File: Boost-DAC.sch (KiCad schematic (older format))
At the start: 26 parts, among them Q17 BSZ100N06NSATMA1, U6 LTC3873, U7 MAX5215

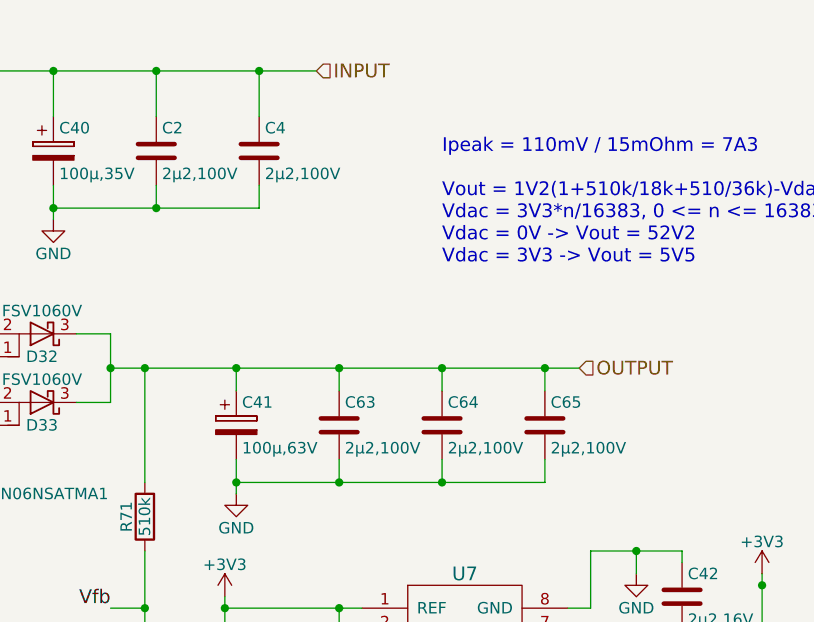
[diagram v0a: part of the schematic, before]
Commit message: 0.2 HW files finalized and repo cleaned up.
-BOM is now up-to-date and available in .csv and .pdf formats
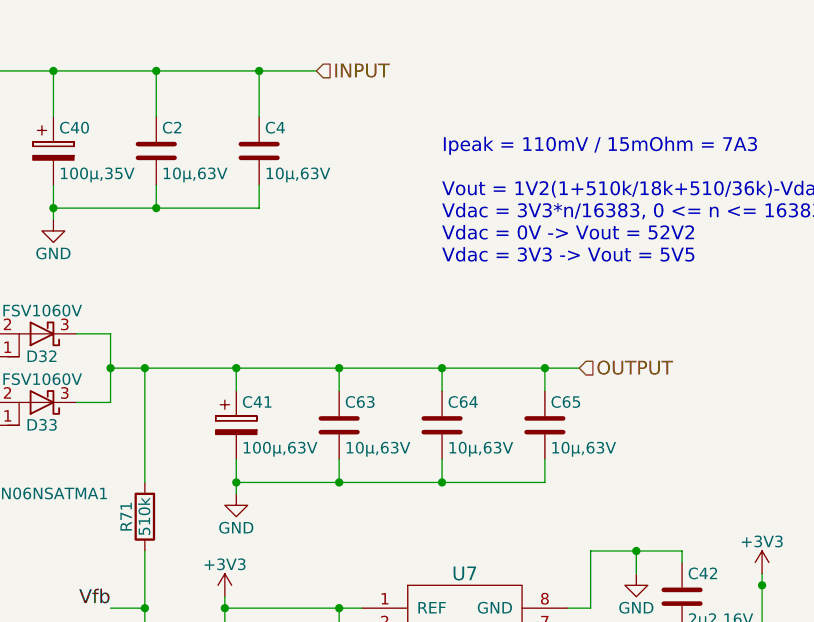
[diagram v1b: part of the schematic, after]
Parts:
- C2, C4, C63, C64, C65: value 2µ2,100V -> 10µ,63V; MFG HMK325B7225MM-P -> ANY
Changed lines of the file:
@@
 P 6450 3550
 F 0 "C63" H 6475 3650 50  0000 L CNN
-F 1 "2µ2,100V" H 6475 3450 50  0000 L CNN
+F 1 "10µ,63V" H 6475 3450 50  0000 L CNN
 F 2 "Capacitors_SMD:C_1210" H 6488 3400 50  0001 C CNN
 F 3 "" H 6450 3550 50  0001 C CNN
-F 4 "HMK325B7225MM-P" H 6450 3550 60  0001 C CNN "MFG"
+F 4 "ANY" H 6450 3550 60  0001 C CNN "MFG"
 F 5 "X7R" H 6450 3550 60  0001 C CNN "TempCo."
 	1    6450 3550
@@
 P 6900 3550
 F 0 "C64" H 6925 3650 50  0000 L CNN
-F 1 "2µ2,100V" H 6925 3450 50  0000 L CNN
+F 1 "10µ,63V" H 6925 3450 50  0000 L CNN
 F 2 "Capacitors_SMD:C_1210" H 6938 3400 50  0001 C CNN
 F 3 "" H 6900 3550 50  0001 C CNN
-F 4 "HMK325B7225MM-P" H 6900 3550 60  0001 C CNN "MFG"
+F 4 "ANY" H 6900 3550 60  0001 C CNN "MFG"
 F 5 "X7R" H 6900 3550 60  0001 C CNN "TempCo."
 	1    6900 3550
@@
 P 7350 3550
 F 0 "C65" H 7375 3650 50  0000 L CNN
-F 1 "2µ2,100V" H 7375 3450 50  0000 L CNN
+F 1 "10µ,63V" H 7375 3450 50  0000 L CNN
 F 2 "Capacitors_SMD:C_1210" H 7388 3400 50  0001 C CNN
 F 3 "" H 7350 3550 50  0001 C CNN
-F 4 "HMK325B7225MM-P" H 7350 3550 60  0001 C CNN "MFG"
+F 4 "ANY" H 7350 3550 60  0001 C CNN "MFG"
 F 5 "X7R" H 7350 3550 60  0001 C CNN "TempCo."
 	1    7350 3550
@@
 P 5650 2350
 F 0 "C2" H 5675 2450 50  0000 L CNN
-F 1 "2µ2,100V" H 5675 2250 50  0000 L CNN
+F 1 "10µ,63V" H 5675 2250 50  0000 L CNN
 F 2 "Capacitors_SMD:C_1210" H 5688 2200 50  0001 C CNN
 F 3 "" H 5650 2350 50  0001 C CNN
-F 4 "HMK325B7225MM-P" H 5650 2350 60  0001 C CNN "MFG"
+F 4 "ANY" H 5650 2350 60  0001 C CNN "MFG"
 F 5 "X7R" H 5650 2350 60  0001 C CNN "TempCo."
 	1    5650 2350
@@
 P 6100 2350
 F 0 "C4" H 6125 2450 50  0000 L CNN
-F 1 "2µ2,100V" H 6125 2250 50  0000 L CNN
+F 1 "10µ,63V" H 6125 2250 50  0000 L CNN
 F 2 "Capacitors_SMD:C_1210" H 6138 2200 50  0001 C CNN
 F 3 "" H 6100 2350 50  0001 C CNN
-F 4 "HMK325B7225MM-P" H 6100 2350 60  0001 C CNN "MFG"
+F 4 "ANY" H 6100 2350 60  0001 C CNN "MFG"
 F 5 "X7R" H 6100 2350 60  0001 C CNN "TempCo."
 	1    6100 2350
